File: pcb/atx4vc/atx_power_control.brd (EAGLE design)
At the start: 86 x 70 mm, 61 parts, among them IC2 REG1117, IC3 STM32F042F4, IC4 MY_7905DT, J1 ATX24RH, SW1 324_SW, SW2 324_SW, SW3 324_SW, SW4 324_SW, SW5 324_SW, SW6 324_SW, SW7 324_SW, U1 USBC_16P, U2 USBC_16P

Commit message: updated pcb
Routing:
- net GND: track 26.9 -> 57.1 mm
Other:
- board text added: "ATX4VC.COM dekuNukem SEPT 2022 PT4"
- board text removed: "ATX4VC.COM dekuNukem SEPT 2022 PT3"
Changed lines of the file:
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@@
 <text x="6.096" y="35.052" size="2.54" layer="26" rot="MR90" align="center">ATX4VC.COM
 dekuNukem SEPT 2022
-PT3</text>
+PT4</text>
 <text x="43.9712" y="42.7944" size="1.1684" layer="25" align="center">GND</text>
 <text x="41.3042" y="48.0014" size="1.143" layer="25" align="center">3V3</text>
@@
 <text x="54.864" y="9.525" size="1.27" layer="25" rot="R180" align="center">BRIGHT</text>
 <text x="57.404" y="20.574" size="1.27" layer="25" rot="R90" align="center">FAN SPD</text>
-<rectangle x1="66.04" y1="8.763" x2="74.549" y2="18.923" layer="41"/>
+<rectangle x1="66.167" y1="6.477" x2="74.676" y2="16.637" layer="41"/>
+<rectangle x1="79.883" y1="0.127" x2="87.63" y2="63.627" layer="41"/>
+<rectangle x1="79.883" y1="0.127" x2="87.63" y2="63.627" layer="42"/>
 </plain>
 <attributes>
@@
 <contactref element="U1" pad="B11A12"/>
 <contactref element="U1" pad="P$13"/>
+<wire x1="82.804" y1="27.178" x2="76.234" y2="27.178" width="1.27" layer="1"/>
+<wire x1="76.234" y1="27.178" x2="75.599" y2="26.543" width="1.27" layer="1"/>
+<wire x1="82.804" y1="37.338" x2="76.084" y2="37.338" width="1.27" layer="1"/>
+<wire x1="76.084" y1="37.338" x2="75.449" y2="36.703" width="1.27" layer="1"/>
+<wire x1="82.804" y1="47.498" x2="75.957" y2="47.498" width="1.27" layer="1"/>
+<wire x1="75.957" y1="47.498" x2="75.449" y2="46.99" width="1.27" layer="1"/>
+<wire x1="82.804" y1="57.658" x2="75.957" y2="57.658" width="1.27" layer="1"/>
+<wire x1="75.957" y1="57.658" x2="75.449" y2="57.15" width="1.27" layer="1"/>
 </signal>
 <signal name="+3V3">
@@
 <mfgpreviewcolor name="substratecolor" color="0xFF786E46"/>
 </mfgpreviewcolors>
+<errors>
+</errors>
 </board>
 </drawing>

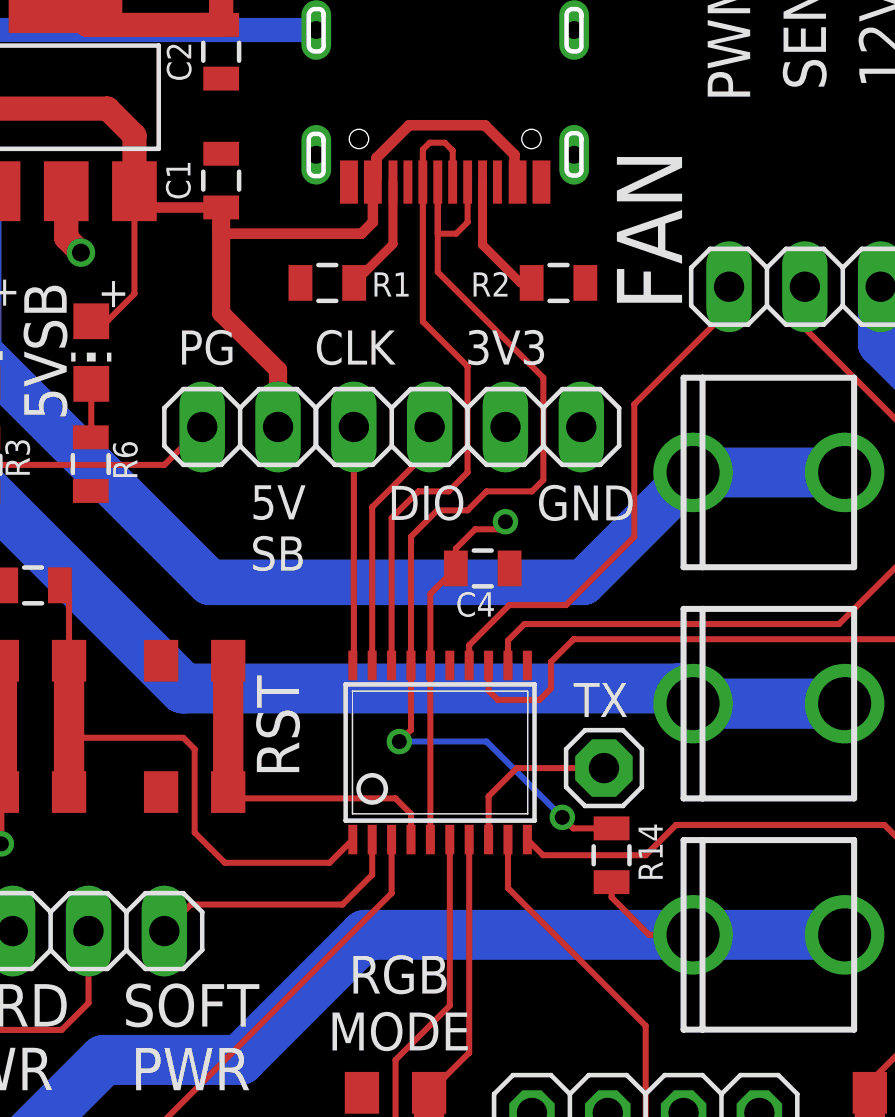
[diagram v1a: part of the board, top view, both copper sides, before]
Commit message: fixed led board silkscreen, changed ATX4VC to use PG signal
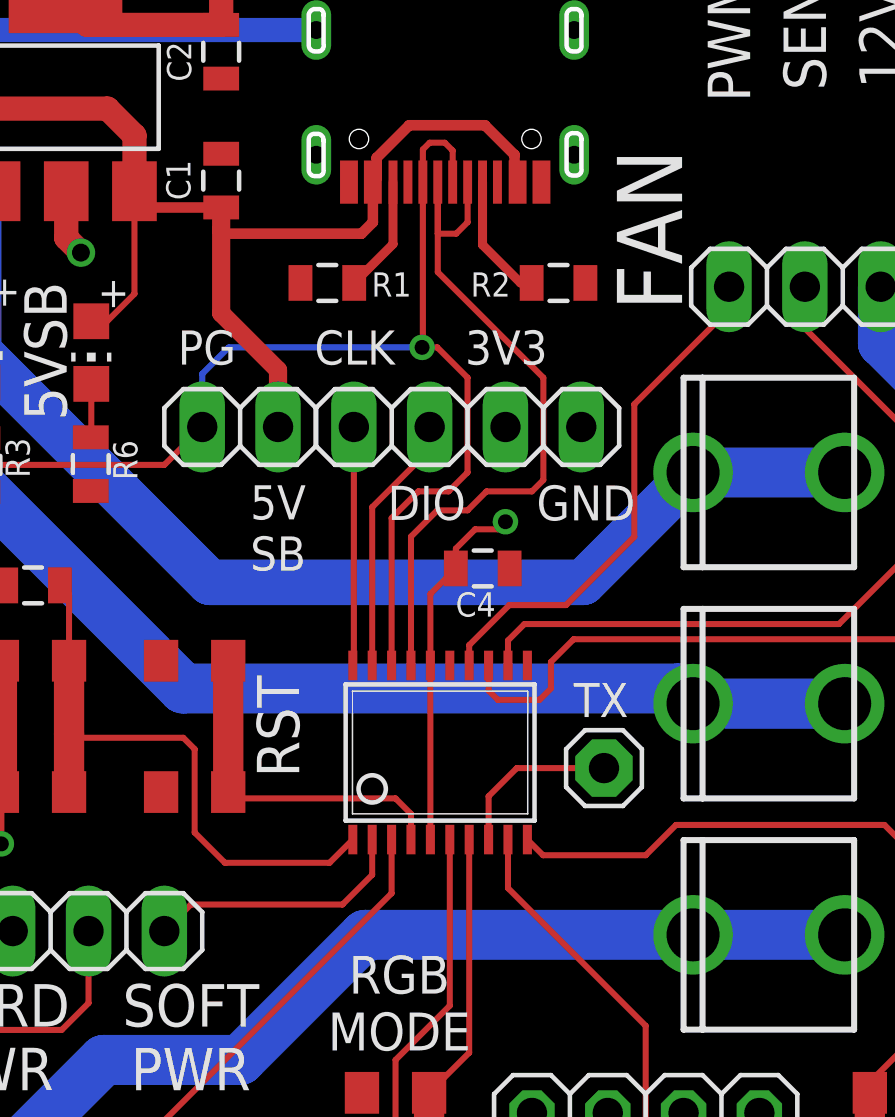
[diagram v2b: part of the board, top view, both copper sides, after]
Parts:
- removed R14: 5.1K, joyAnalog:0805
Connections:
- removed net N$12: F3.1, F3.2, J1.1, J1.12, J1.13, J1.2, R14.1
- removed net USB_DP: IC3.18, U2.A6, U2.B6
- new net N$14: F3.1, F3.2, J1.1, J1.12, J1.13, J1.2
- net N$28: now also IC3.18, U2.A6, U2.B6
- net USB_DN: no longer R14.2
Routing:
- net N$12: track 106.0 -> 0.00 mm
- net N$14: track 0.00 -> 102.2 mm
- net N$28: track 24.8 -> 56.5 mm, vias 0 -> 1
- net USB_DP: track 21.8 -> 0.00 mm
- net USB_DN: track 36.2 -> 25.2 mm, vias 2 -> 0
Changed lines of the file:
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@@
 <attribute name="NAME" x="60.7695" y="57.912" size="0.8128" layer="25" rot="R90"/>
-</element>
-<element name="R14" library="joyAnalog" package="0805" value="5.1K" x="44.831" y="30.988" smashed="yes" rot="R90">
-<attribute name="NAME" x="46.5455" y="30.099" size="0.8128" layer="25" rot="R90"/>
 </element>
 </elements>
@@
 <wire x1="38.76" y1="39.7452" x2="38.76" y2="37.3488" width="0.2032" layer="1"/>
 </signal>
-<signal name="USB_DP">
-<contactref element="U2" pad="A6"/>
-<contactref element="U2" pad="B6"/>
-<contactref element="IC3" pad="18"/>
-<wire x1="38.507" y1="53.5445" x2="38.507" y2="54.636" width="0.2032" layer="1"/>
-<wire x1="38.507" y1="54.636" x2="38.735" y2="54.864" width="0.2032" layer="1"/>
-<wire x1="38.735" y1="54.864" x2="39.243" y2="54.864" width="0.2032" layer="1"/>
-<wire x1="39.507" y1="54.6" x2="39.507" y2="53.5445" width="0.2032" layer="1"/>
-<wire x1="39.243" y1="54.864" x2="39.507" y2="54.6" width="0.2032" layer="1"/>
-<wire x1="38.507" y1="53.5445" x2="38.507" y2="48.869" width="0.2032" layer="1"/>
-<wire x1="38.507" y1="48.869" x2="40.005" y2="47.371" width="0.2032" layer="1"/>
-<wire x1="40.005" y1="47.371" x2="40.005" y2="43.815" width="0.2032" layer="1"/>
-<wire x1="40.005" y1="43.815" x2="39.37" y2="43.18" width="0.2032" layer="1"/>
-<wire x1="39.37" y1="43.18" x2="38.354" y2="43.18" width="0.2032" layer="1"/>
-<wire x1="38.354" y1="43.18" x2="37.46" y2="42.286" width="0.2032" layer="1"/>
-<wire x1="37.46" y1="42.286" x2="37.46" y2="37.3488" width="0.2032" layer="1"/>
-</signal>
 <signal name="N$31">
 <contactref element="R1" pad="1"/>
@@
 <wire x1="38.989" y1="42.545" x2="38.11" y2="41.666" width="0.2032" layer="1"/>
 <wire x1="38.11" y1="41.666" x2="38.11" y2="37.3488" width="0.2032" layer="1"/>
-<contactref element="R14" pad="2"/>
-<wire x1="44.831" y1="31.888" x2="43.55" y2="31.888" width="0.2032" layer="1"/>
-<wire x1="43.55" y1="31.888" x2="43.18" y2="32.258" width="0.2032" layer="1"/>
-<via x="43.18" y="32.258" extent="1-16" drill="0.5"/>
-<wire x1="43.18" y1="32.258" x2="40.64" y2="34.798" width="0.2032" layer="16"/>
-<wire x1="40.64" y1="34.798" x2="37.719" y2="34.798" width="0.2032" layer="16"/>
-<via x="37.719" y="34.798" extent="1-16" drill="0.5"/>
-<wire x1="37.719" y1="34.798" x2="38.11" y2="35.189" width="0.2032" layer="1"/>
-<wire x1="38.11" y1="35.189" x2="38.11" y2="37.3488" width="0.2032" layer="1"/>
 </signal>
 <signal name="BUTTON1">
@@
 <wire x1="65.876" y1="19.532" x2="65.786" y2="19.442" width="0.508" layer="1"/>
 </signal>
-<signal name="N$12">
-<contactref element="J1" pad="1"/>
-<contactref element="J1" pad="13"/>
-<contactref element="J1" pad="12"/>
-<contactref element="J1" pad="2"/>
-<contactref element="F3" pad="1"/>
-<contactref element="F3" pad="2"/>
-<wire x1="14.014" y1="58.1" x2="12.38" y2="58.1" width="1.6764" layer="16"/>
-<wire x1="12.38" y1="58.1" x2="7.874" y2="53.594" width="1.6764" layer="16"/>
-<wire x1="7.874" y1="53.594" x2="7.874" y2="19.685" width="1.6764" layer="16"/>
-<wire x1="11.459" y1="16.1" x2="14.014" y2="16.1" width="1.6764" layer="16"/>
-<wire x1="7.874" y1="19.685" x2="11.459" y2="16.1" width="1.6764" layer="16"/>
-<wire x1="14.014" y1="16.1" x2="14.014" y2="11.9" width="1.6764" layer="16"/>
-<wire x1="14.014" y1="11.9" x2="19.514" y2="11.9" width="1.6764" layer="16"/>
-<wire x1="19.514" y1="11.9" x2="20.784" y2="11.9" width="1.6764" layer="16"/>
-<wire x1="47.5615" y1="28.321" x2="52.6415" y2="28.321" width="1.6764" layer="16"/>
-<wire x1="20.784" y1="11.9" x2="22.987" y2="14.103" width="1.6764" layer="16"/>
-<wire x1="22.987" y1="14.103" x2="22.987" y2="19.304" width="1.6764" layer="16"/>
-<wire x1="27.813" y1="24.13" x2="32.385" y2="24.13" width="1.6764" layer="16"/>
-<wire x1="32.385" y1="24.13" x2="36.576" y2="28.321" width="1.6764" layer="16"/>
-<wire x1="36.576" y1="28.321" x2="47.5615" y2="28.321" width="1.6764" layer="16"/>
-<wire x1="22.987" y1="19.304" x2="27.813" y2="24.13" width="1.6764" layer="16"/>
-<contactref element="R14" pad="1"/>
-<wire x1="44.831" y1="30.088" x2="44.831" y2="29.58" width="0.2032" layer="1"/>
-<wire x1="46.09" y1="28.321" x2="44.831" y2="29.58" width="0.2032" layer="1"/>
-<wire x1="46.09" y1="28.321" x2="47.5615" y2="28.321" width="0.2032" layer="1"/>
-</signal>
 <signal name="N$8">
 <contactref element="LED4" pad="C"/>
@@
 <wire x1="31.115" y1="45.339" x2="29.845" y2="44.069" width="0.2032" layer="1"/>
 <wire x1="29.845" y1="44.069" x2="22.098" y2="44.069" width="0.2032" layer="1"/>
+<contactref element="U2" pad="A6"/>
+<contactref element="U2" pad="B6"/>
+<contactref element="IC3" pad="18"/>
+<wire x1="38.507" y1="53.5445" x2="38.507" y2="54.636" width="0.2032" layer="1"/>
+<wire x1="38.507" y1="54.636" x2="38.735" y2="54.864" width="0.2032" layer="1"/>
+<wire x1="38.735" y1="54.864" x2="39.243" y2="54.864" width="0.2032" layer="1"/>
+<wire x1="39.507" y1="54.6" x2="39.507" y2="53.5445" width="0.2032" layer="1"/>
+<wire x1="39.243" y1="54.864" x2="39.507" y2="54.6" width="0.2032" layer="1"/>
+<wire x1="40.005" y1="43.815" x2="39.37" y2="43.18" width="0.2032" layer="1"/>
+<wire x1="39.37" y1="43.18" x2="38.354" y2="43.18" width="0.2032" layer="1"/>
+<wire x1="38.354" y1="43.18" x2="37.46" y2="42.286" width="0.2032" layer="1"/>
+<wire x1="37.46" y1="42.286" x2="37.46" y2="37.3488" width="0.2032" layer="1"/>
+<wire x1="31.115" y1="45.339" x2="31.115" y2="47.117" width="0.2032" layer="16"/>
+<wire x1="31.115" y1="47.117" x2="32.004" y2="48.006" width="0.2032" layer="16"/>
+<wire x1="32.004" y1="48.006" x2="38.481" y2="48.006" width="0.2032" layer="16"/>
+<via x="38.481" y="48.006" extent="1-16" drill="0.5"/>
+<wire x1="40.005" y1="46.99" x2="40.005" y2="43.815" width="0.2032" layer="1"/>
+<wire x1="38.507" y1="53.5445" x2="38.507" y2="48.032" width="0.2032" layer="1"/>
+<wire x1="38.507" y1="48.032" x2="38.481" y2="48.006" width="0.2032" layer="1"/>
+<wire x1="38.481" y1="48.006" x2="38.989" y2="48.006" width="0.2032" layer="1"/>
+<wire x1="38.989" y1="48.006" x2="40.005" y2="46.99" width="0.2032" layer="1"/>
 </signal>
 <signal name="N$6">
@@
 <wire x1="66.04" y1="52.197" x2="66.79" y2="52.197" width="0.2032" layer="1"/>
 </signal>
+<signal name="N$14">
+<contactref element="J1" pad="1"/>
+<contactref element="J1" pad="13"/>
+<contactref element="J1" pad="12"/>
+<contactref element="J1" pad="2"/>
+<contactref element="F3" pad="1"/>
+<contactref element="F3" pad="2"/>
+<wire x1="14.014" y1="58.1" x2="12.38" y2="58.1" width="1.6764" layer="16"/>
+<wire x1="12.38" y1="58.1" x2="7.874" y2="53.594" width="1.6764" layer="16"/>
+<wire x1="7.874" y1="53.594" x2="7.874" y2="19.685" width="1.6764" layer="16"/>
+<wire x1="11.459" y1="16.1" x2="14.014" y2="16.1" width="1.6764" layer="16"/>
+<wire x1="7.874" y1="19.685" x2="11.459" y2="16.1" width="1.6764" layer="16"/>
+<wire x1="14.014" y1="16.1" x2="14.014" y2="11.9" width="1.6764" layer="16"/>
+<wire x1="14.014" y1="11.9" x2="19.514" y2="11.9" width="1.6764" layer="16"/>
+<wire x1="19.514" y1="11.9" x2="20.784" y2="11.9" width="1.6764" layer="16"/>
+<wire x1="47.5615" y1="28.321" x2="52.6415" y2="28.321" width="1.6764" layer="16"/>
+<wire x1="20.784" y1="11.9" x2="22.987" y2="14.103" width="1.6764" layer="16"/>
+<wire x1="22.987" y1="14.103" x2="22.987" y2="19.304" width="1.6764" layer="16"/>
+<wire x1="27.813" y1="24.13" x2="32.385" y2="24.13" width="1.6764" layer="16"/>
+<wire x1="32.385" y1="24.13" x2="36.576" y2="28.321" width="1.6764" layer="16"/>
+<wire x1="36.576" y1="28.321" x2="47.5615" y2="28.321" width="1.6764" layer="16"/>
+<wire x1="22.987" y1="19.304" x2="27.813" y2="24.13" width="1.6764" layer="16"/>
+</signal>
 </signals>

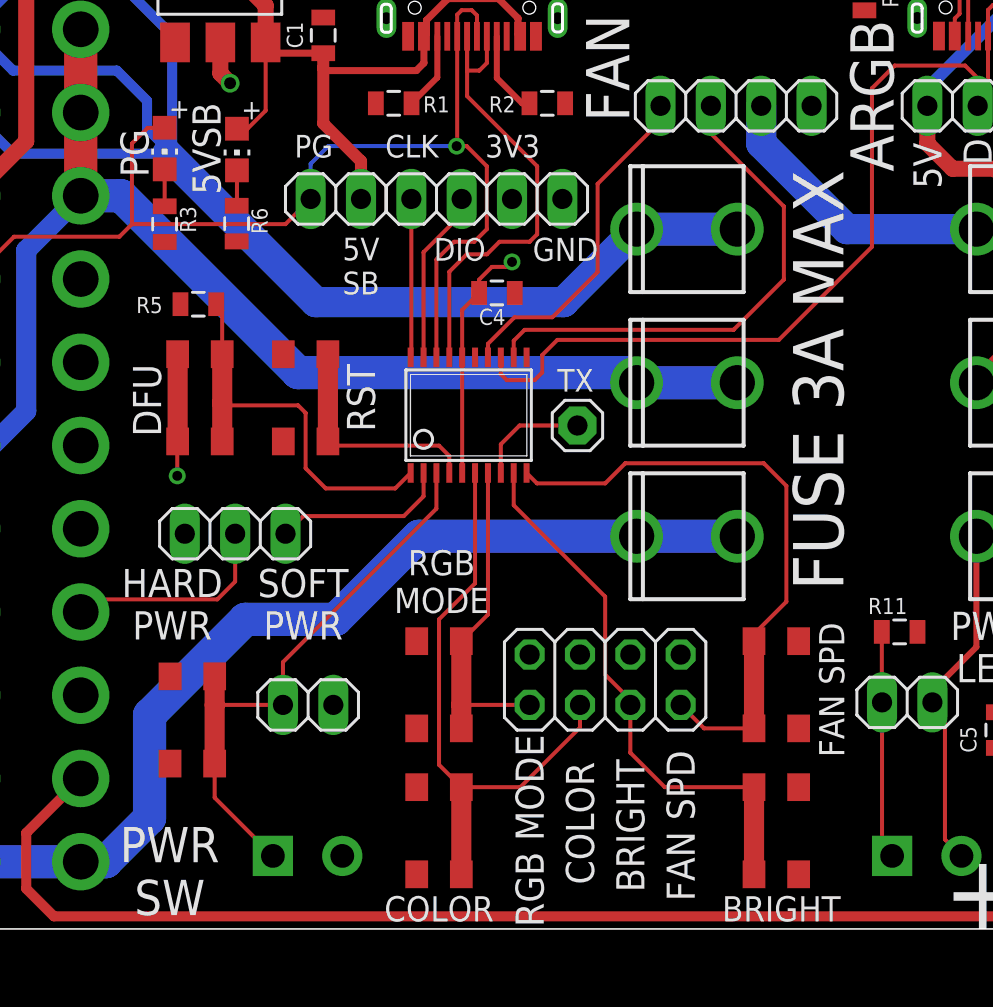
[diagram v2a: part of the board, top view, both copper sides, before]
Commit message: added UART RX header, brightness button shared with DFU button
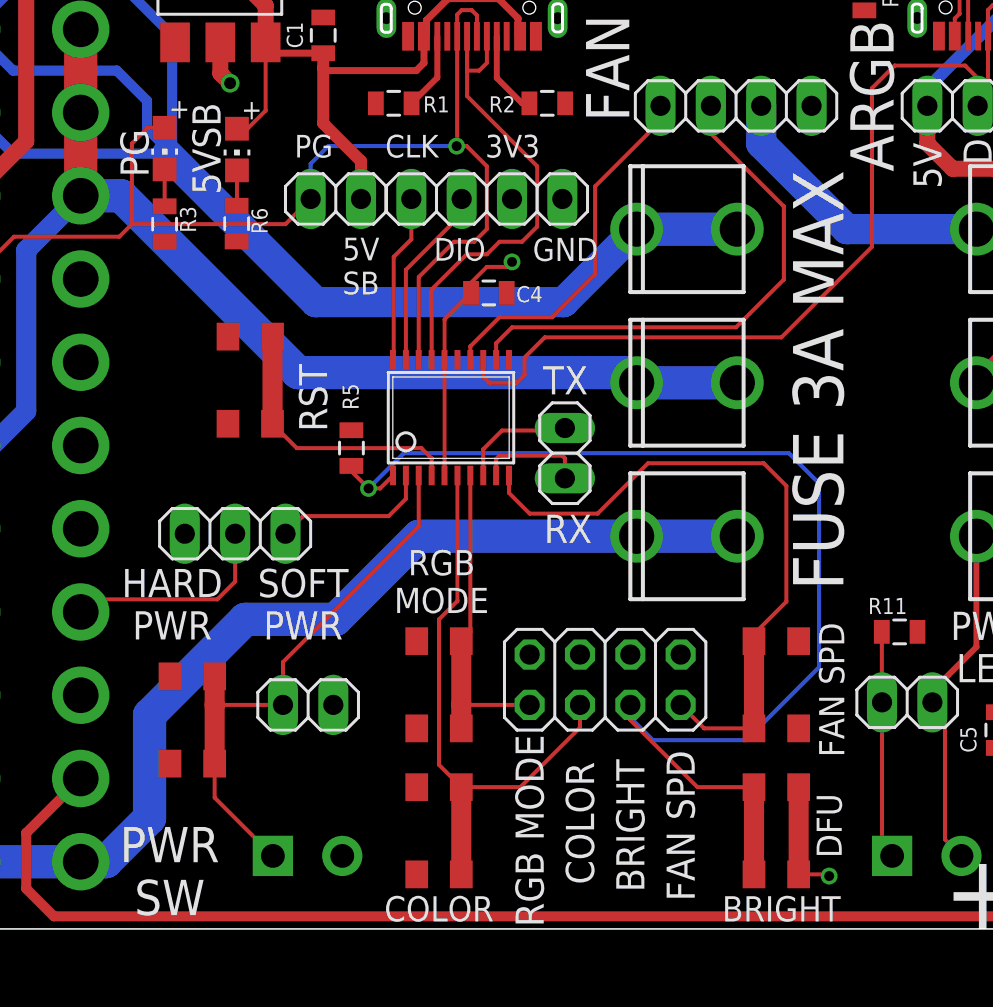
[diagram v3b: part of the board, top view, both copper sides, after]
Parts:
- removed SW6: 324_SW, 3pos_slide_switch_centered:342_SWICH_FOOT
- JP10: device adafruit_changed:1X01 -> pinhead:1X02
- moved SW4 36.4 mm to (54.6, 13.5), turned to 90 degrees
- moved R5 10.6 mm to (33.2, 32.8), turned to 270 degrees
- moved SW3 2.93 mm to (28.1, 36.2)
- moved JP10 1.53 mm to (43.9, 32.5), turned to 270 degrees
- moved IC3 0.90 mm to (38.2, 34.3)
- moved C4 0.41 mm to (40.1, 40.6)
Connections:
- removed net N$30: IC3.9, JP9.4, SW6.P$1, SW6.P$4
- new net N$12: IC3.9, JP10.2
- net +3V3: now also JP9.3
- net BUTTON2: now also JP9.4
- net GND: no longer JP9.3, SW6.P$2, SW6.P$3
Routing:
- net BUTTON2: track 20.3 -> 61.3 mm, vias 0 -> 1
- net N$30: track 27.9 -> 0.00 mm
- net N$12: track 0.00 -> 5.44 mm
- net N$27: track 31.3 -> 33.9 mm
- net BUTTON1: track 11.7 -> 14.0 mm
- net N$35: track 46.0 -> 47.0 mm
- net N$24: track 8.93 -> 7.98 mm
- net N$7: track 17.4 -> 18.4 mm
- net N$6: track 26.0 -> 27.0 mm
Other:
- board text added: "RX"
